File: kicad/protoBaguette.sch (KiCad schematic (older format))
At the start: 28 parts

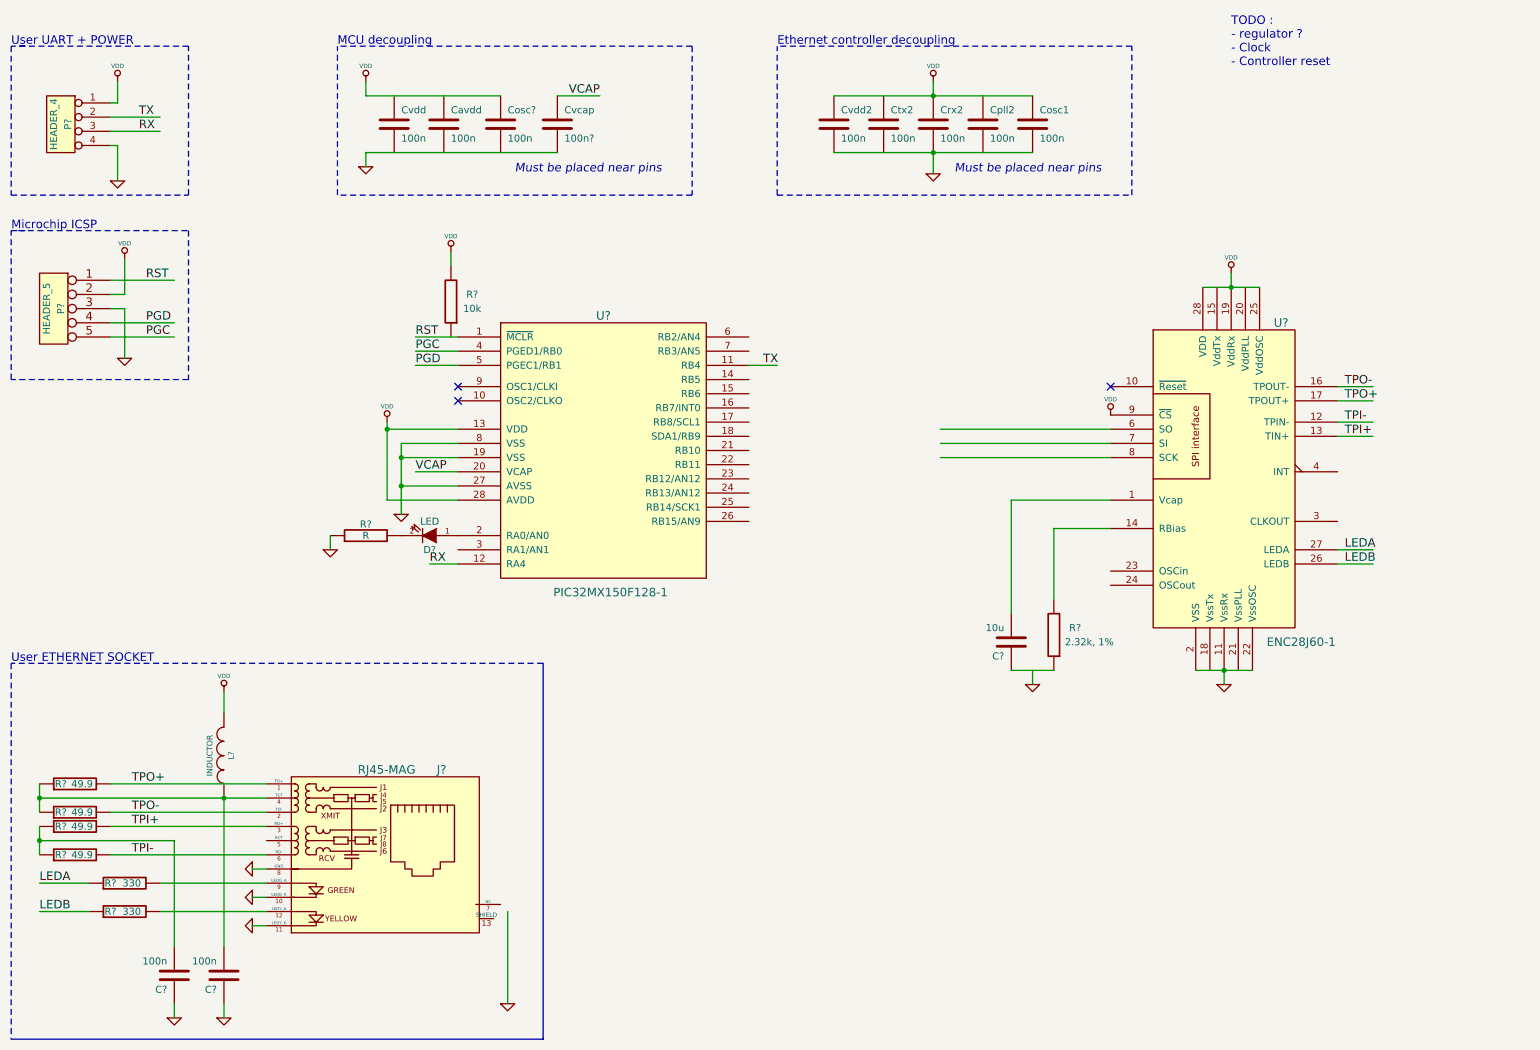
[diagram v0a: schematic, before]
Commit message: Suppr fichiers binaires Modif sch
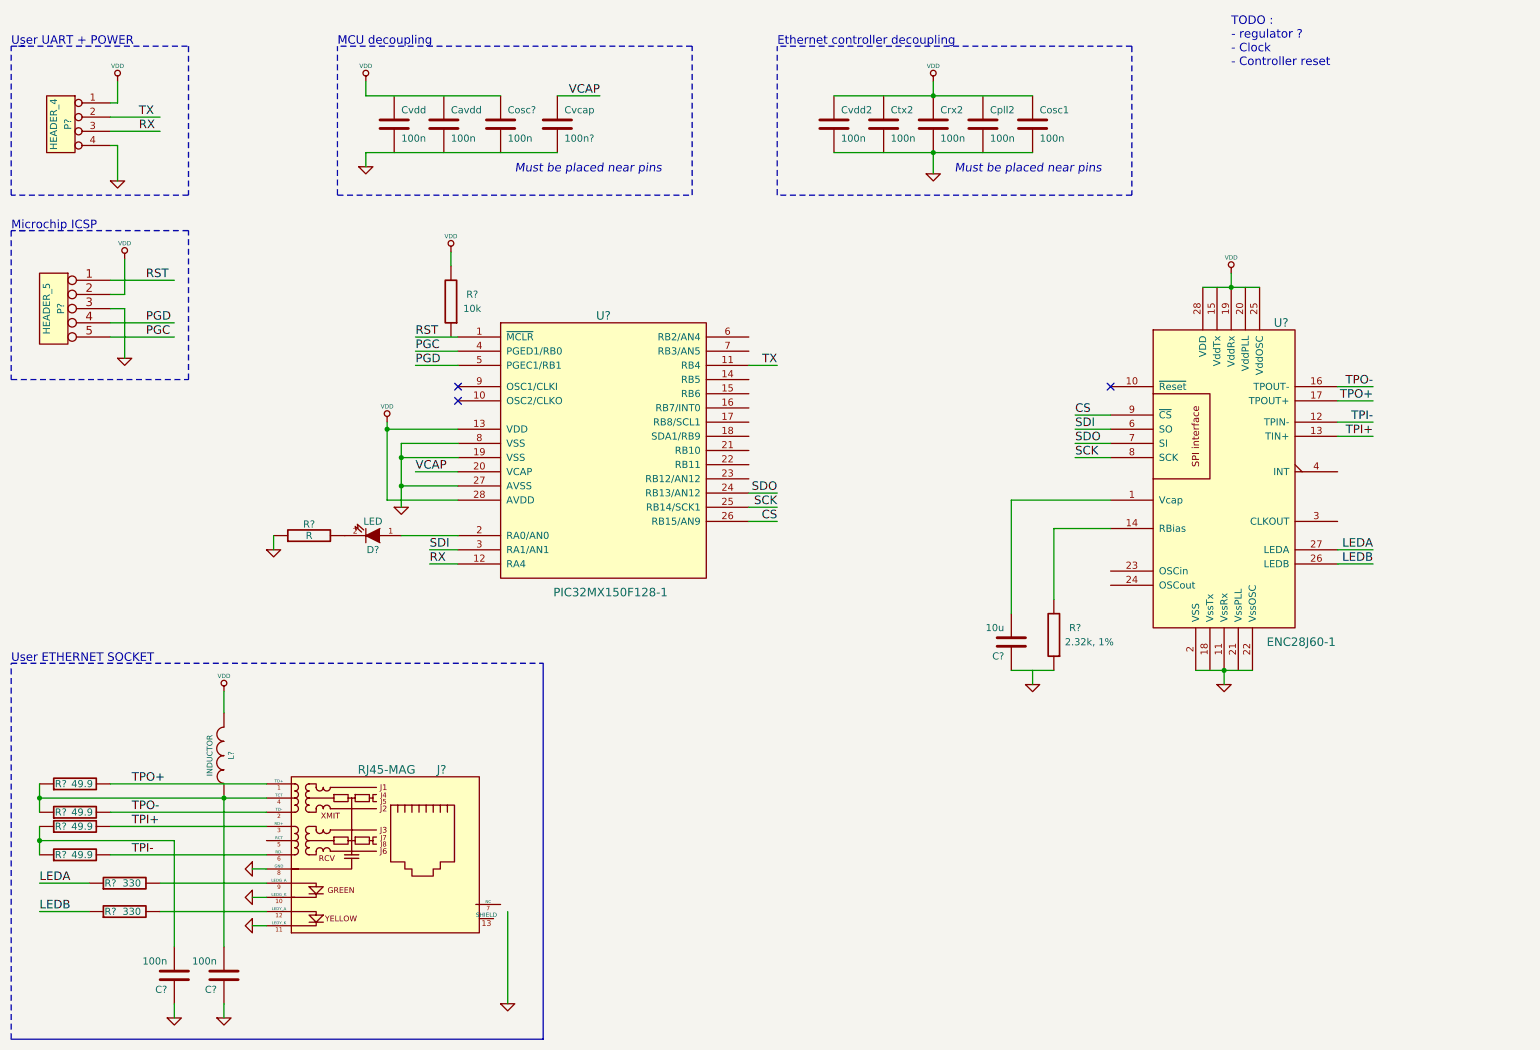
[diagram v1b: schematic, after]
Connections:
- net labels added: CS, SCK, SDI, SDO
- wire segments 77 -> 83
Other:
- moved on the sheet: D?, R?

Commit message: First try, not satisfying. New routing iteration needed.
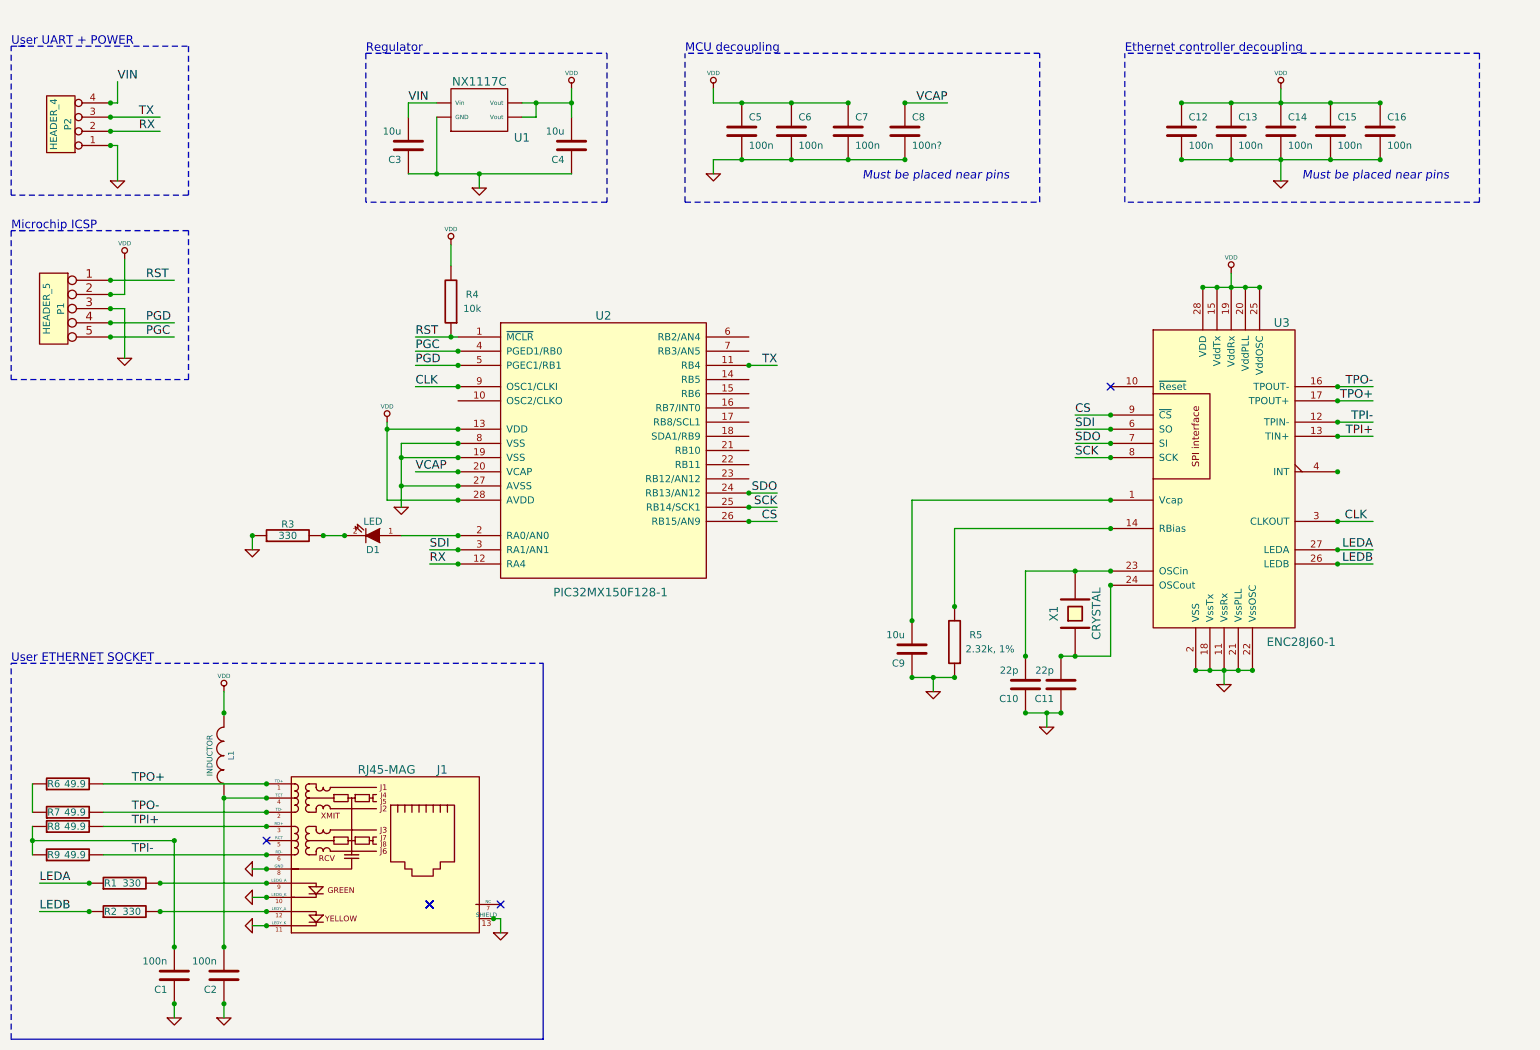
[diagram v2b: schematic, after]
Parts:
- removed R? (x4): 49.9, symbol R
- added C10, C11: 22p, symbol C
- added C3, C4: 10u, symbol C
- added R6, R7, R8, R9: 49.9, symbol R
- added U1: NX1117C, symbol NX1117C
- added X1: CRYSTAL, symbol CRYSTAL
- R3: renamed from R?; value R -> 330
- gave numbers to parts that had none: 15
- renumbered Cvdd2 to C12, Ctx2 to C13, Crx2 to C14, Cpll2 to C15, Cosc1 to C16, Cvdd to C5, Cavdd to C6, Cvcap to C8
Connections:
- net labels added: CLK, VIN
- wire segments 83 -> 102
- no-connect marks 3 -> 8
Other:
- note added: "Regulator"
- note removed: "TODO : \n- regulator ?\n- Clock\n- Controller reset\n"
- moved on the sheet: C12, C13, C14, C15, C16, C5, C6, C7, C8, C9, R3, R5

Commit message: Final layout, before footprint inspection
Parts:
- added P3, P4: HEADER_5, symbol HEADER_5
- added PWR1, RX1, TX1: LED, symbol LED
- added R10, R11, R12: 330, symbol R
- renumbered D1 to OK1
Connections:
- net labels added: BO14, BO15, BO16, BO17, BO18, BO6, BO7
- wire segments 102 -> 131
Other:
- note added: "MCU breakout"
- moved on the sheet: C12, C13, C14, C15, C16, C3, C4, C5, C6, C7, C8, OK1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

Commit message: First batch, as ordered to Seeed !
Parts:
- C8: value 100n? -> 10u
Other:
- note added: "Notes : \n- Intnernal MCU clock can be use to drive controller \nby connecting a breakout pin to quartz pin\n- Controller clock (from quartz) can drive MCU if\n high timing accuracy is needed"
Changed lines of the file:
@@
-EESchema Schematic File Version 2  date dim. 09 juin 2013 16:31:18 CEST
+EESchema Schematic File Version 2  date dim. 09 juin 2013 19:38:13 CEST
 LIBS:power
 LIBS:device
@@
 encoding utf-8
 Sheet 1 1
-Title "Alpha prototype"
+Title "ProtoBaguette, first board"
 Date "9 jun 2013"
-Rev "0.1"
-Comp "ProtoBaguette"
+Rev "1.0"
+Comp "Hexabread"
 Comment1 ""
 Comment2 ""
@@
 Comment4 ""
 $EndDescr
+Text Notes 7200 6100 0    60   ~ 0
+Notes : \n- Intnernal MCU clock can be use to drive controller \nby connecting a breakout pin to quartz pin\n- Controller clock (from quartz) can drive MCU if\n high timing accuracy is needed
 Wire Wire Line
 	1400 2850 1400 2500
@@
 P 7500 1250
 F 0 "C8" H 7550 1350 50  0000 L CNN
-F 1 "100n?" H 7550 1150 50  0000 L CNN
+F 1 "10u" H 7550 1150 50  0000 L CNN
 	1    7500 1250
 	1    0    0    -1
